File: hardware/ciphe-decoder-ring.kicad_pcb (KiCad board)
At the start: 2 copper layers, 70 x 70 mm, 35 parts, among them SW1 EC11E09244BS, U1 XIAO-RP2040-DIP

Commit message: Added preview and instructions
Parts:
- added ? (x4): , Graphics, F.Cu at (-34.0, -51.4)
- added ? (x5): , Graphics, B.Cu at (35.1, -35.6)
- added ?: , Graphics, F.Cu at (35.1, -35.6)
- added ?: , Graphics, B.Cu at (-34.0, -51.4)
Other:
- board text added: "5V"
- board text added: "GND"
- board text added: "LED"
- board text added: "ROT-A"
- board text added: "ROT-B"
- board text added: "SW1"
- board text added: "Steven Smethurst (@funvill) 2025-Feb-26 github.com/funvill/ciphe-decoder-ring-pcb"
- board text removed: "Created by: Steven Smethurst (@funvill) 2025-Feb-26"

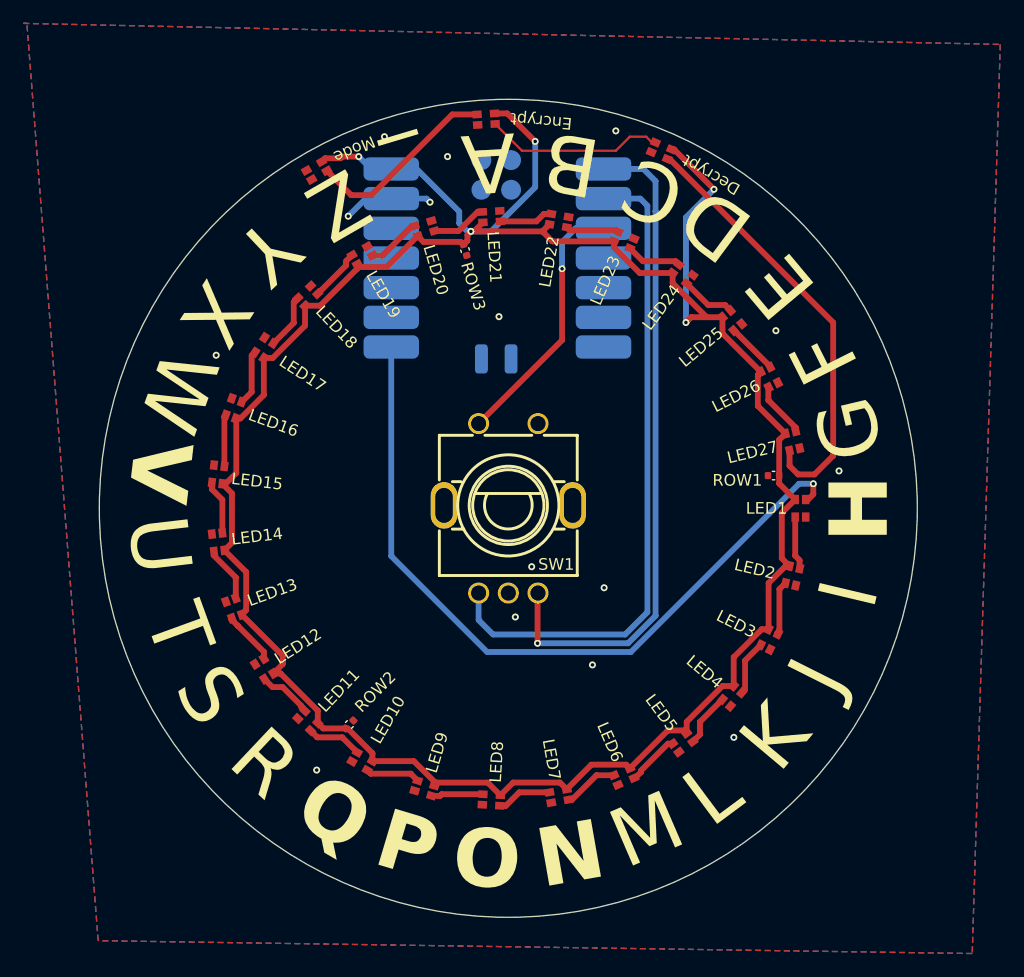
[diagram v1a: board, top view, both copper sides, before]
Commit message: Rotated the letters, Added 3D models to 3D viewer
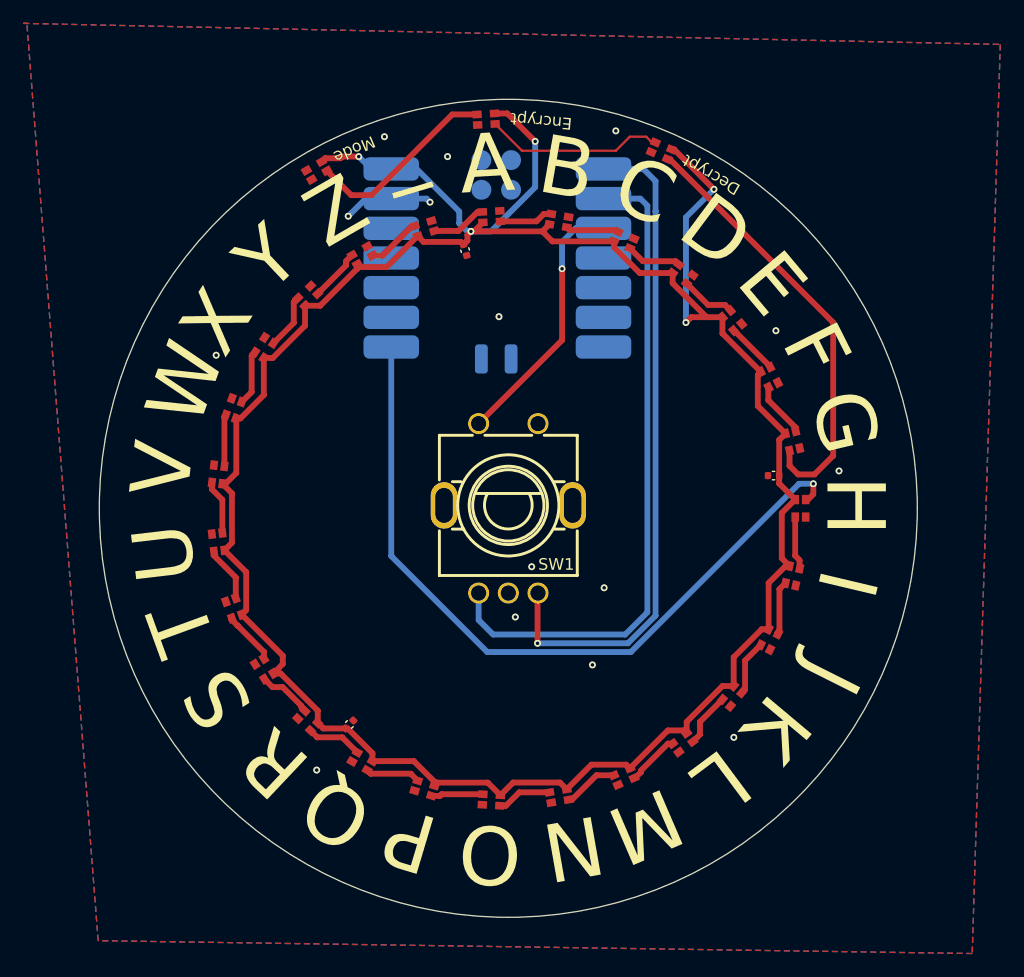
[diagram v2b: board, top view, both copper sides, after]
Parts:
- moved ? 4.16 mm to (31.8, -38.0), turned to -175 degrees
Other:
- board text removed: "Steven Smethurst (@funvill) 2025-Feb-26 github.com/funvill/ciphe-decoder-ring-pcb"

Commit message: As manufacured with JLCPCB on 2025-Feb-27
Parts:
- added R1: 470, Resistor_SMD:R_0402_1005Metric, F.Cu at (-10.0, -6.24)
- added R2: 5.1k, Resistor_SMD:R_0402_1005Metric, F.Cu at (3.00, 10.0)
- added R3: 5.1k, Resistor_SMD:R_0402_1005Metric, F.Cu at (-3.00, 10.0)
- added TP1: TestPoint, TestPoint:TestPoint_Pad_D1.5mm, B.Cu at (-10.0, -8.25)
- added TP2: TestPoint, TestPoint:TestPoint_Pad_D1.5mm, B.Cu at (-10.0, -4.25)
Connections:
- U1 pad 8: LED_IN -> Net-(U1-GPIO1/RX)
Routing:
- net +5V: track 223.9 -> 247.5 mm
- net Net-(U1-GPIO1/RX): track 0.00 -> 7.06 mm, vias 0 -> 1
- net LED_IN: track 65.1 -> 58.7 mm, vias 1 -> 2
- net Net-(U1-GPIO27/ADC1/A1): track 56.9 -> 57.2 mm, vias 0 -> 1
